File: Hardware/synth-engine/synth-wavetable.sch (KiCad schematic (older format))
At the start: 30 parts

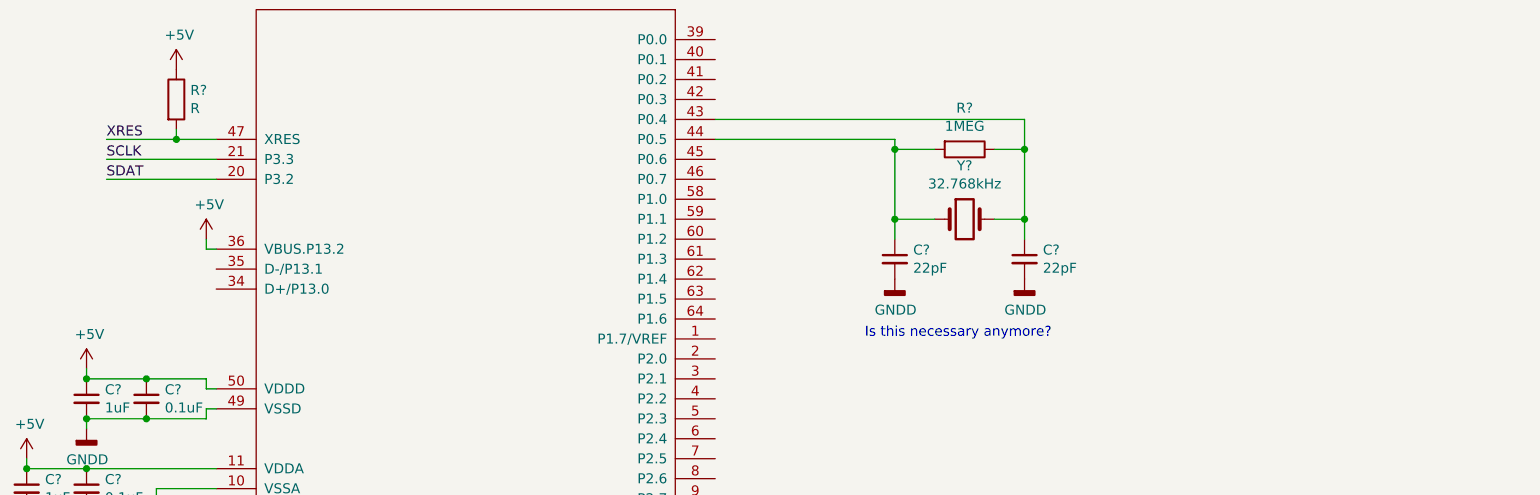
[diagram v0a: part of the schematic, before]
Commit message: add USB connector to Cypress schematic page
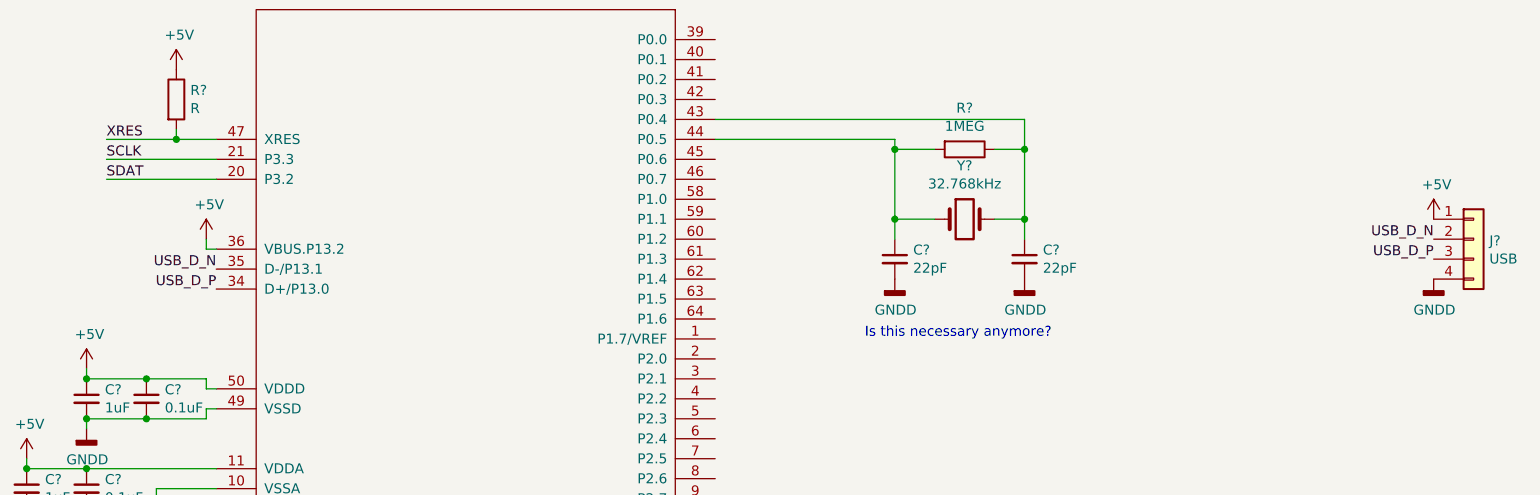
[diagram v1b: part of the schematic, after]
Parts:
- added J?: USB, symbol Connector_Generic:Conn_01x04
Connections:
- net +5V: now also J?.1 (Pin_1)
- net GNDD: now also J?.4 (Pin_4)
- net USB_D_P: now reaches U?.34 (D+/P13.0)
- net USB_D_P: now also J?.3 (Pin_3)
- net USB_D_N: now reaches U?.35 (D-/P13.1)
- net USB_D_N: now also J?.2 (Pin_2)
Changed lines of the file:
@@
 Text Notes 4850 3150 0    50   ~ 0
 Is this necessary anymore?
+$Comp
+L Connector_Generic:Conn_01x04 J?
+U 1 1 5DD96E79
+P 7900 2650
+F 0 "J?" H 7979 2642 50  0000 L CNN
+F 1 "USB" H 7979 2551 50  0000 L CNN
+F 2 "" H 7900 2650 50  0001 C CNN
+F 3 "~" H 7900 2650 50  0001 C CNN
+	1    7900 2650
+	1    0    0    -1
+$EndComp
+$Comp
+L power:+5V #PWR?
+U 1 1 5DD970B4
+P 7700 2550
+F 0 "#PWR?" H 7700 2400 50  0001 C CNN
+F 1 "+5V" H 7715 2723 50  0000 C CNN
+F 2 "" H 7700 2550 50  0001 C CNN
+F 3 "" H 7700 2550 50  0001 C CNN
+	1    7700 2550
+	1    0    0    -1
+$EndComp
+$Comp
+L power:GNDD #PWR?
+U 1 1 5DD9B64B
+P 7700 2850
+F 0 "#PWR?" H 7700 2600 50  0001 C CNN
+F 1 "GNDD" H 7704 2695 50  0000 C CNN
+F 2 "" H 7700 2850 50  0001 C CNN
+F 3 "" H 7700 2850 50  0001 C CNN
+	1    7700 2850
+	1    0    0    -1
+$EndComp
+Text Label 7700 2650 2    50   ~ 0
+USB_D_N
+Text Label 7700 2750 2    50   ~ 0
+USB_D_P
+Text Label 1600 2800 2    50   ~ 0
+USB_D_N
+Text Label 1600 2900 2    50   ~ 0
+USB_D_P
 $EndSCHEMATC

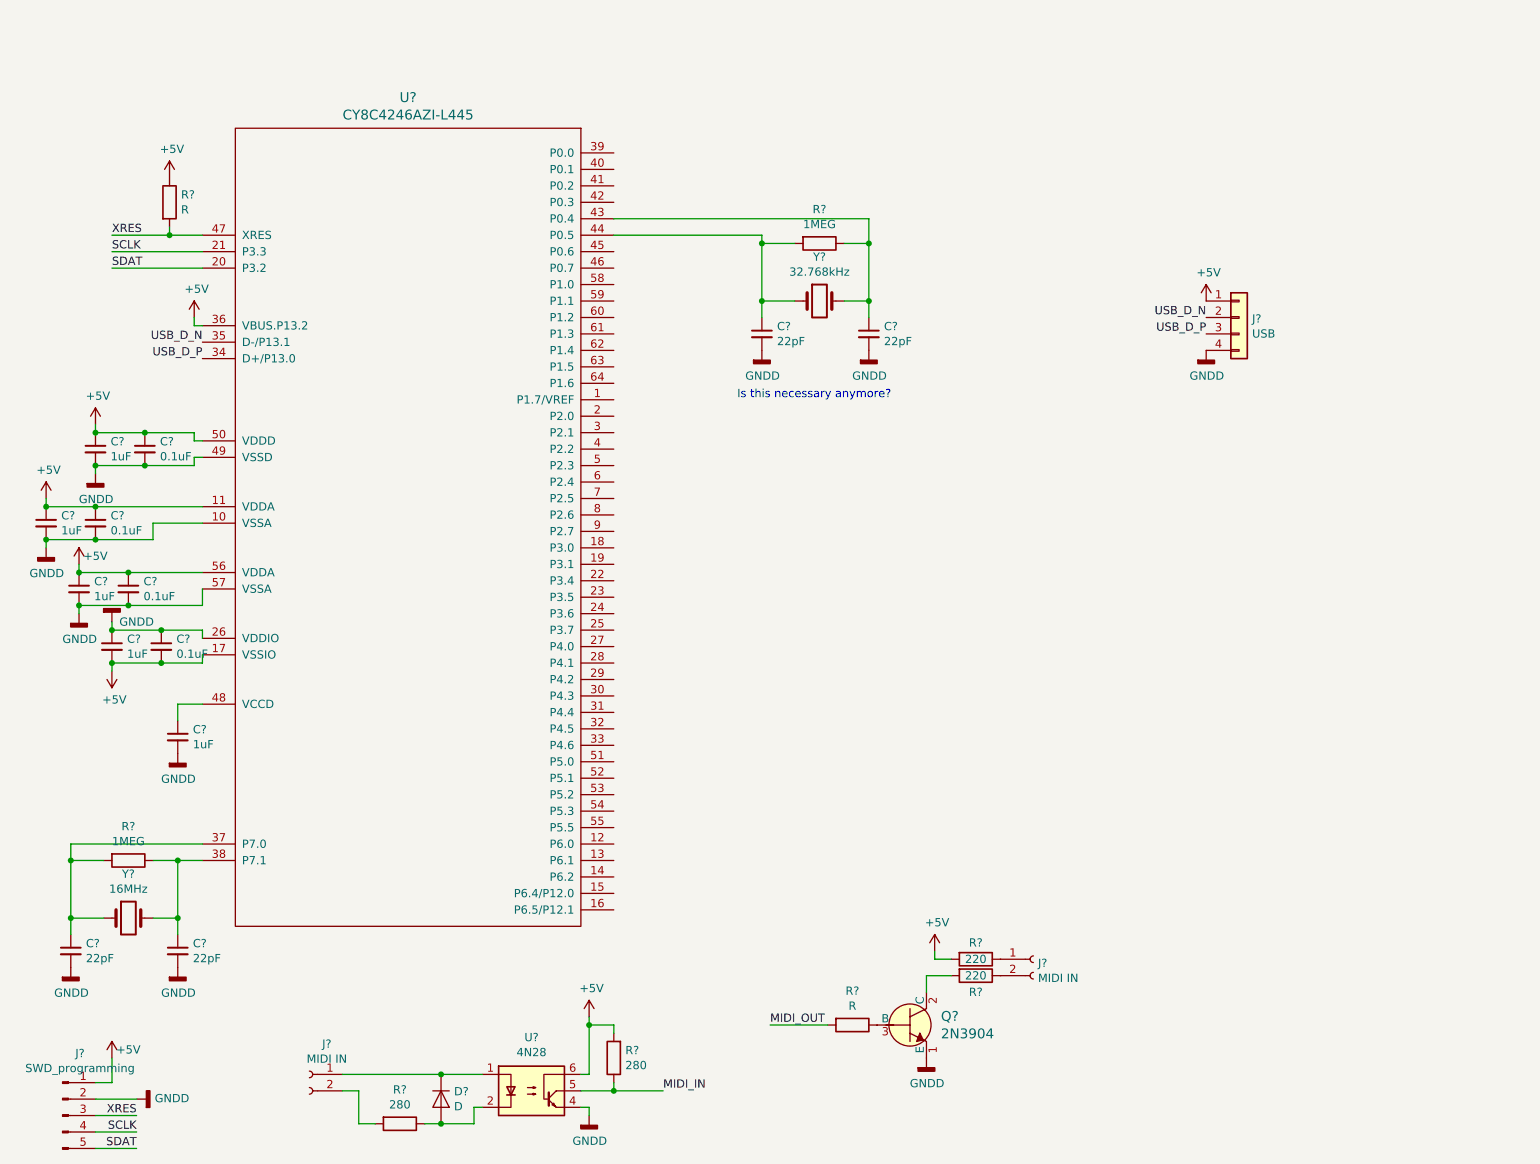
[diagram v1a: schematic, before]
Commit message: add power regulation to schematic
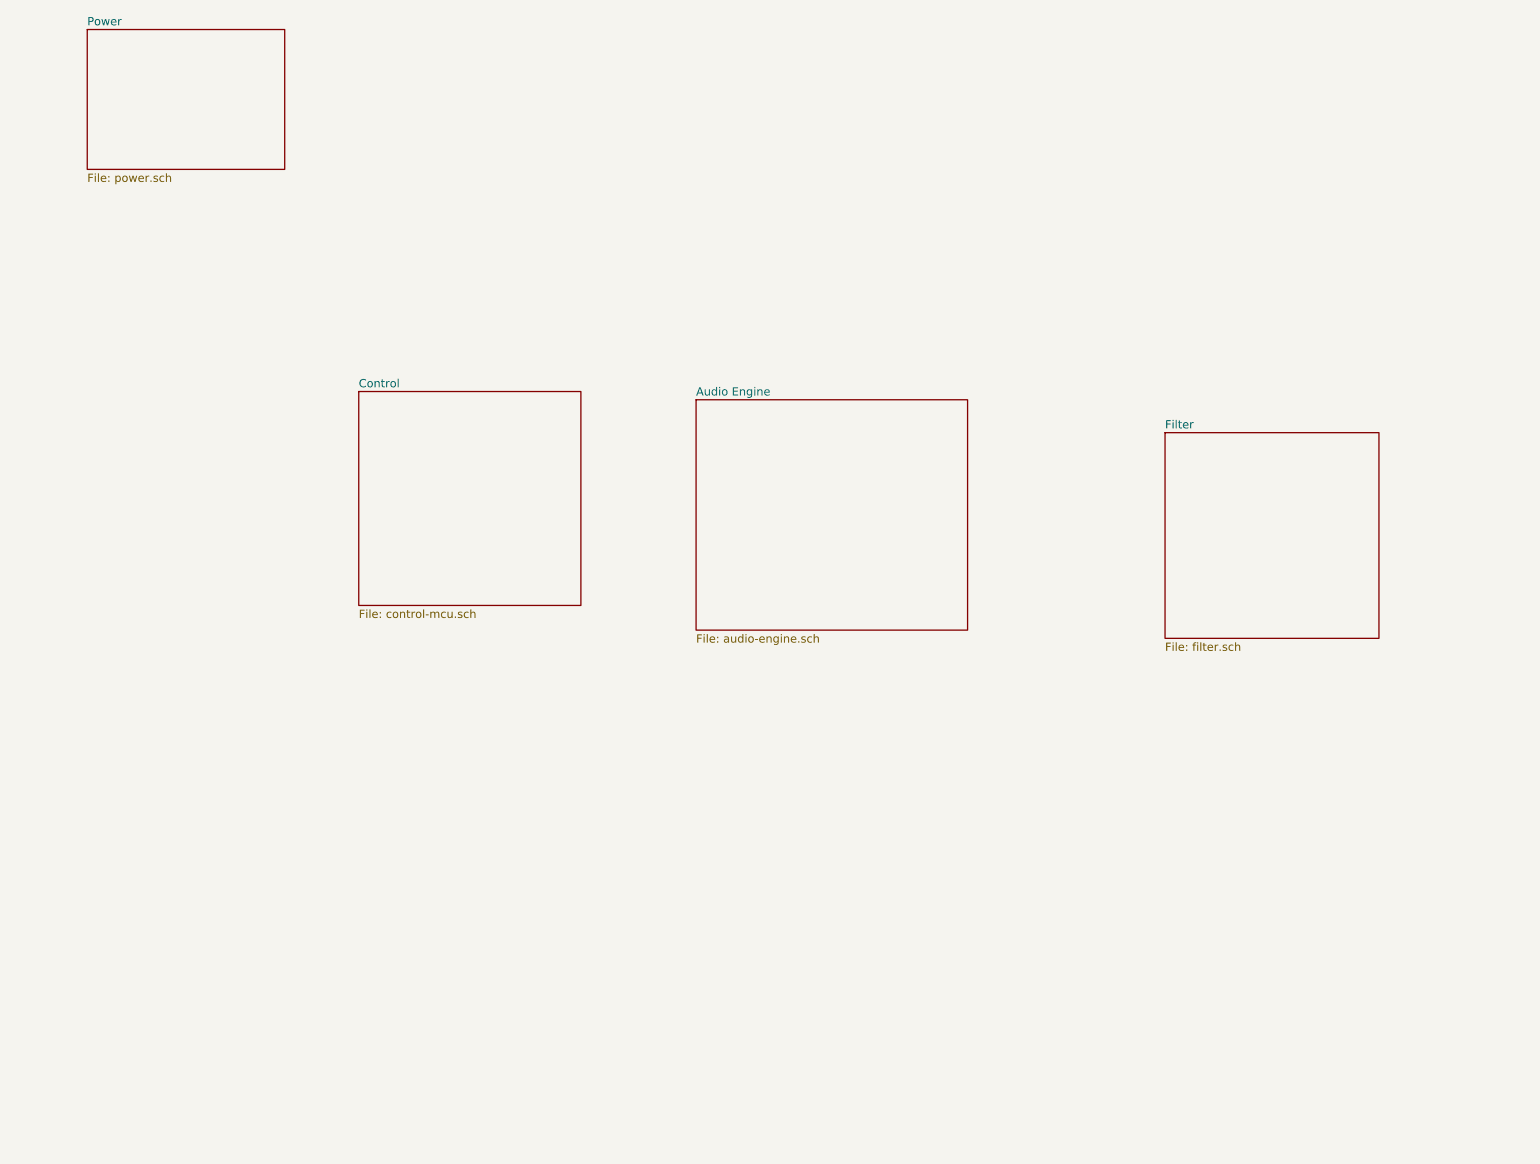
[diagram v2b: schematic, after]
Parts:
- removed C? (x4): 0.1uF, symbol Device:C_Small
- removed C? (x5): 1uF, symbol Device:C_Small
- removed C? (x4): 22pF, symbol Device:C_Small
- removed D?: D, symbol Device:D
- removed J?: SWD_programming, symbol Connector:Conn_01x05_Male
- removed J? (x2): MIDI IN, symbol Connector:Conn_01x02_Female
- removed J?: USB, symbol Connector_Generic:Conn_01x04
- removed Q?: 2N3904, digikey-footprints:TO-92-3, symbol dk_Transistors-Bipolar-BJT-Single:2N3904
- removed R? (x2): R, symbol Device:R
- removed R? (x2): 1MEG, symbol Device:R
- removed R? (x2): 280, symbol Device:R
- removed R? (x2): 220, symbol Device:R
- removed U?: CY8C4246AZI-L445, symbol dac:CY8C4246AZI-L445
- removed U?: 4N28, Package_DIP:DIP-6_W7.62mm, symbol Isolator:4N28
- removed Y?: 16MHz, symbol Device:Crystal
- removed Y?: 32.768kHz, symbol Device:Crystal
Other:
- note removed: "Is this necessary anymore?"

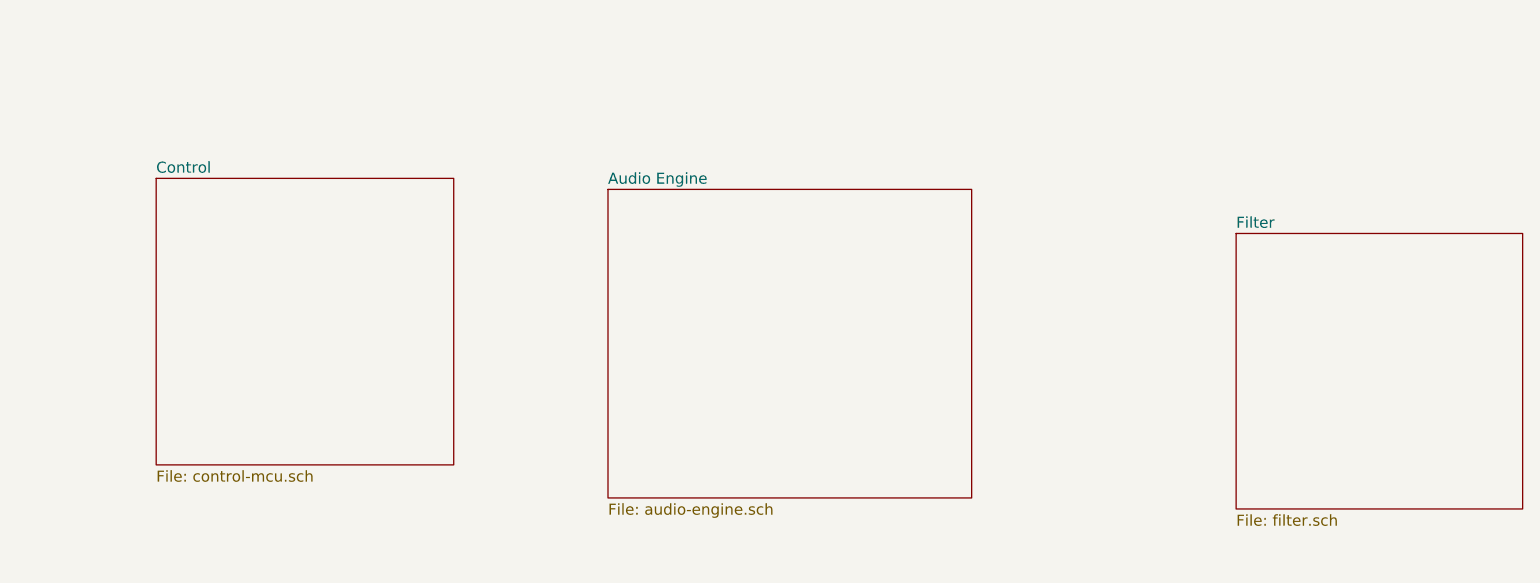
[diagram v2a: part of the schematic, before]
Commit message: add SSI2144 implementation * basically default datasheet version
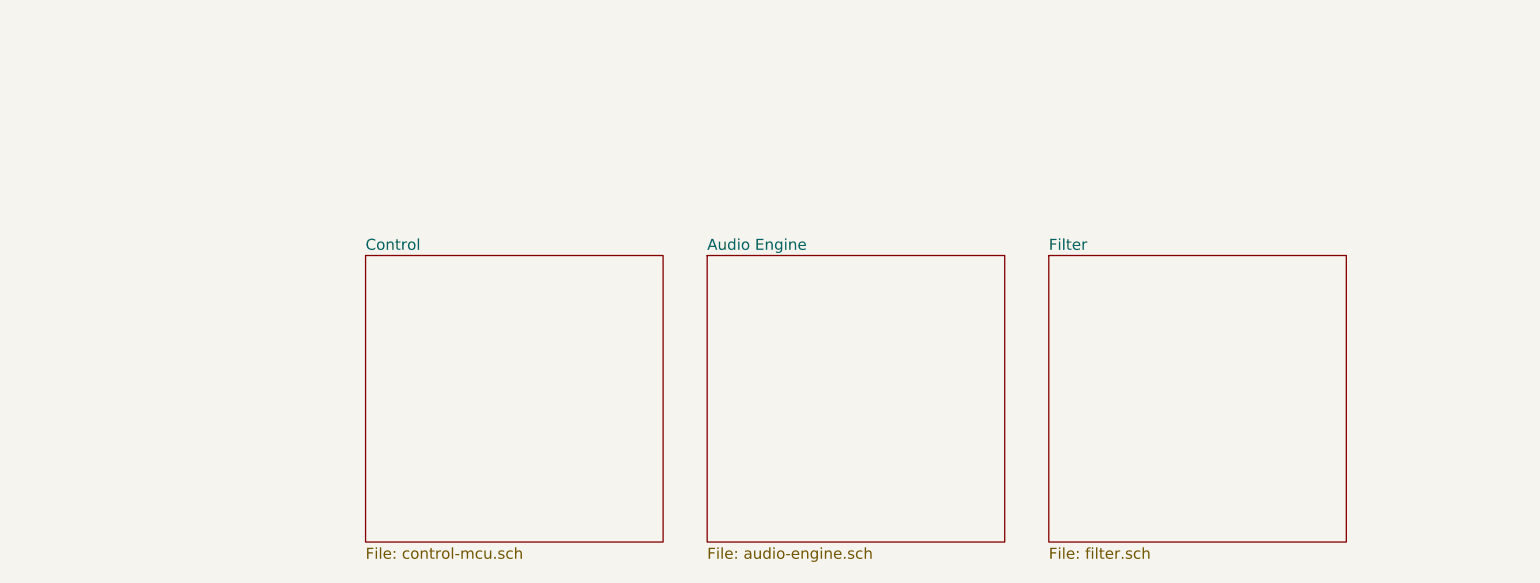
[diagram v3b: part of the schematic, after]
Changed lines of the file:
@@
 $EndDescr
 $Sheet
-S 2550 3100 1350 1300
+S 3500 3450 1350 1300
 U 5DDBDEEA
 F0 "Control" 50
@@
 $EndSheet
 $Sheet
-S 4600 3150 1650 1400
+S 5050 3450 1350 1300
 U 5DDC7BB6
 F0 "Audio Engine" 50
@@
 $EndSheet
 $Sheet
-S 7450 3350 1300 1250
+S 6600 3450 1350 1300
 U 5DDC7E61
 F0 "Filter" 50

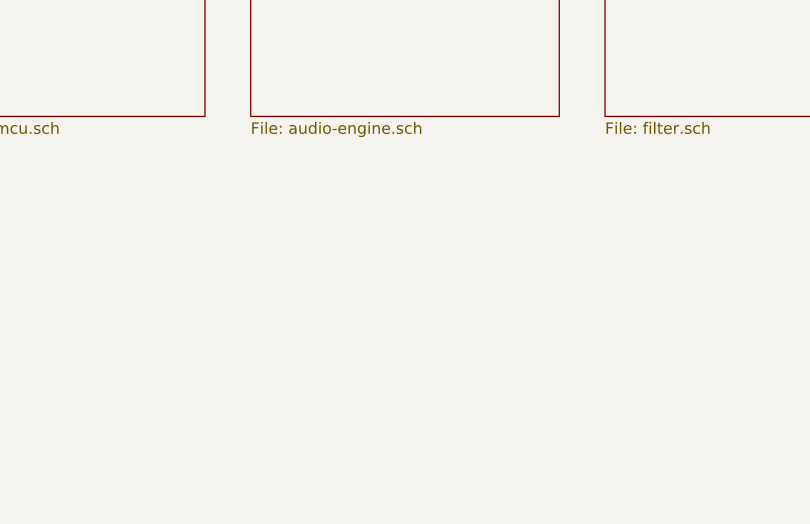
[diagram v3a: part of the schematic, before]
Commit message: add 3.3V analog regulator and add power nets to AK4490
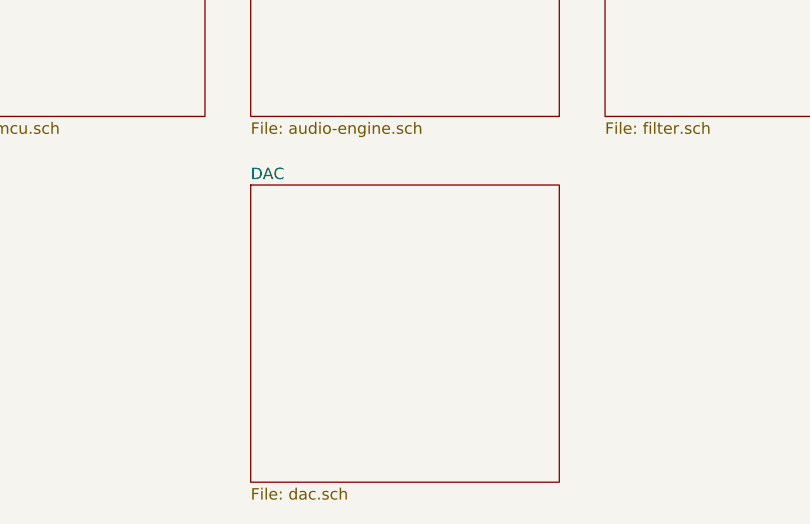
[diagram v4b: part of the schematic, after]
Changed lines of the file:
@@
 $Descr A4 11693 8268
 encoding utf-8
-Sheet 1 5
+Sheet 1 6
 Title ""
 Date ""
@@
 F1 "power.sch" 50
 $EndSheet
+$Sheet
+S 5050 5050 1350 1300
+U 5DD9C8DD
+F0 "DAC" 50
+F1 "dac.sch" 50
+$EndSheet
 $EndSCHEMATC
